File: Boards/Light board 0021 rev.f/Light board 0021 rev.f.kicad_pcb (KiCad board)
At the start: 2 copper layers, 166.4 x 186.7 mm, 43 parts, among them J1 card edge, J2 light connector, Q1 TIP130A, U1 2.2K, U2 2.2K, U3 ULN2003A, U4 ULN2003A, U5 7406, U6 Board Select, U7 6821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

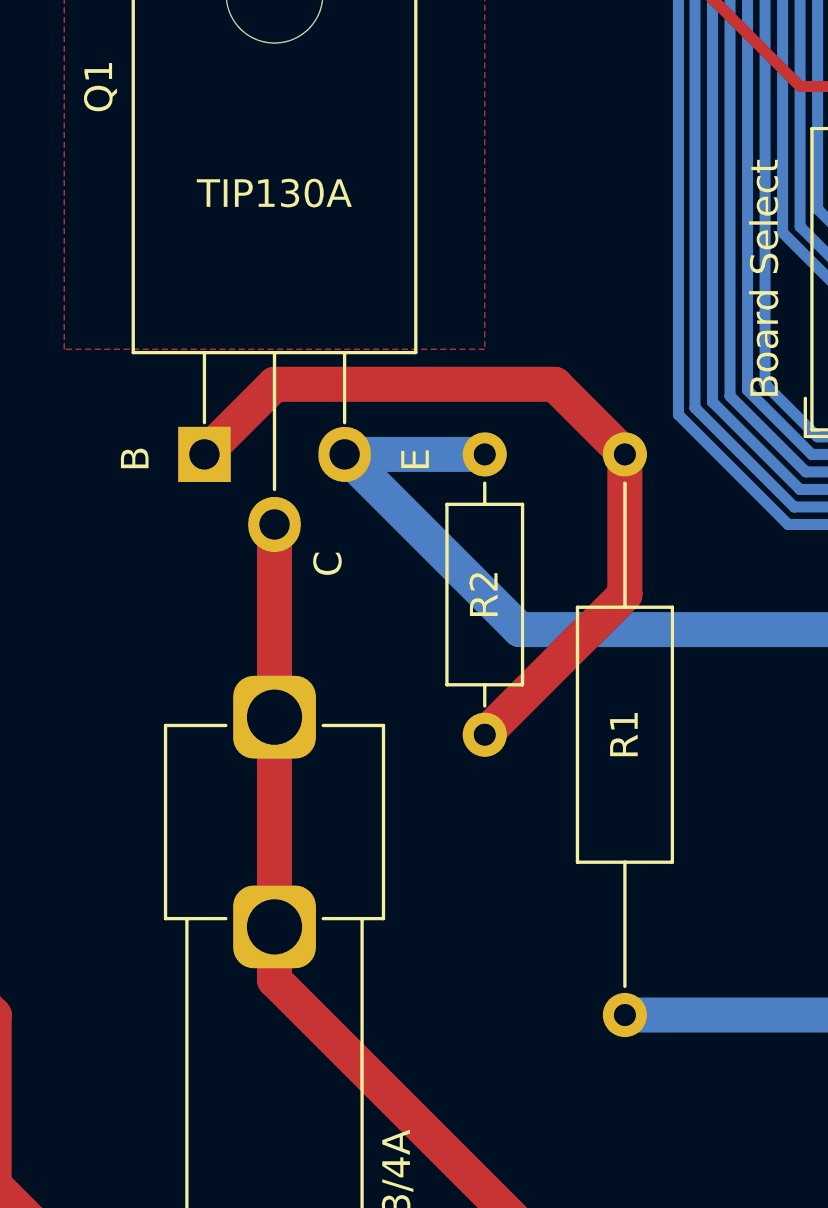
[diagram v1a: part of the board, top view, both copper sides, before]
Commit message: revisions from real life boards
tip130a is actually tip30a, widened holes for crystal, widened holes for big power resistor, fixed cpu board LED resistors
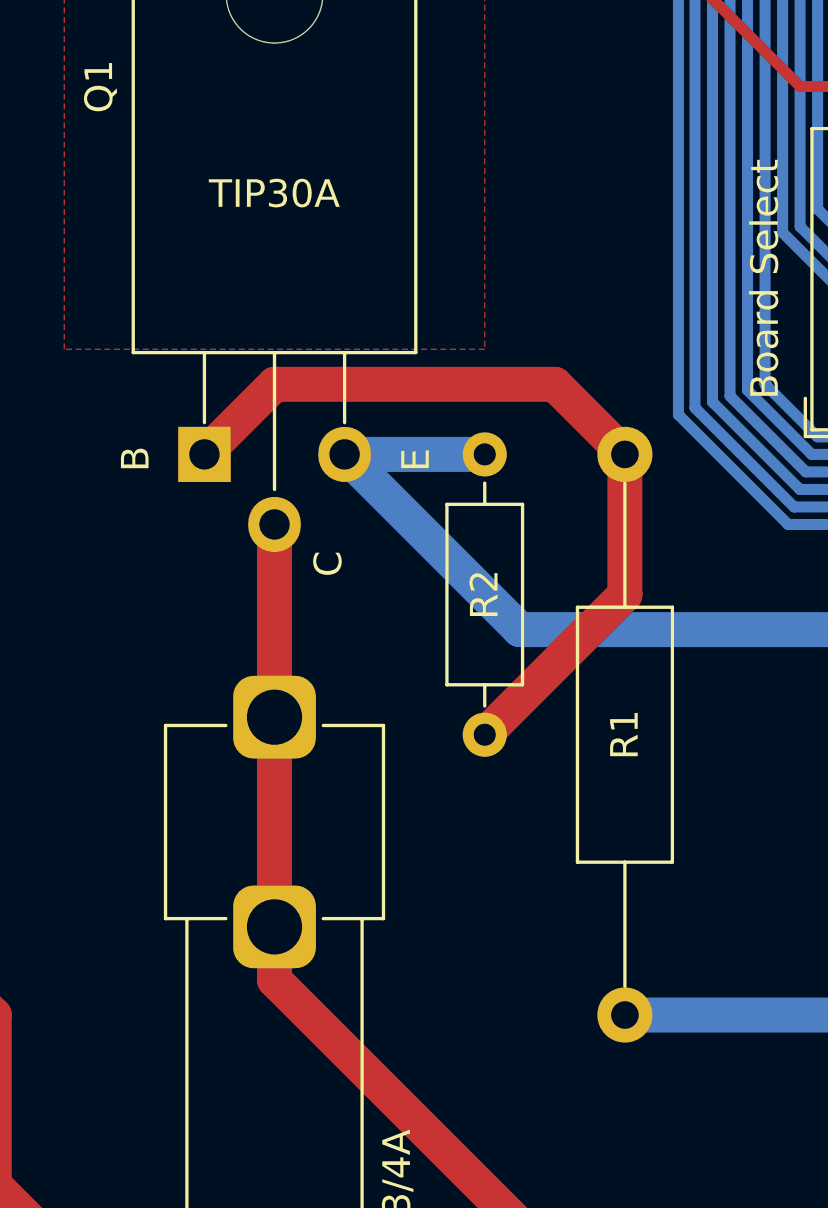
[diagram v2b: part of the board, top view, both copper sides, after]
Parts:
- Q1: value TIP130A -> TIP30A
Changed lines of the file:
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@@
     (fp_line (start 20.32 0) (end 14.66 0)
       (stroke (width 0.1) (type solid)) (layer "F.Fab"))
-    (pad "1" thru_hole circle (at 0 0 270) (size 1.6 1.6) (drill 0.8) (layers "*.Cu" "*.Mask")
+    (pad "1" thru_hole circle (at 0 0 270) (size 2 2) (drill 1) (layers "*.Cu" "*.Mask")
       (net 13 "Net-(Q1-B)") (pintype "passive"))
-    (pad "2" thru_hole oval (at 20.32 0 270) (size 1.6 1.6) (drill 0.8) (layers "*.Cu" "*.Mask")
+    (pad "2" thru_hole circle (at 20.32 0 270) (size 2 2) (drill 1) (layers "*.Cu" "*.Mask")
       (net 101 "Net-(C5-Pad1)") (pintype "passive"))
     (model "${KICAD6_3DMODEL_DIR}/Resistor_THT.3dshapes/R_Axial_DIN0309_L9.0mm_D3.2mm_P20.32mm_Horizontal.wrl"
@@
         (effects (font (size 1 1) (thickness 0.15)))
     )
-    (fp_text value "TIP130A" (at 2.54 -9.435) (layer "F.SilkS")
-        (effects (font (size 1 1) (thickness 0.15)))
-    )
+    (fp_text value "TIP30A" (at 2.54 -9.435) (layer "F.SilkS")
+        (effects (font (size 1 1) (thickness 0.15)))
+    )
